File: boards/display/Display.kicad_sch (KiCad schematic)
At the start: 20 parts, among them J1 FH12-10S-0.5SH(55), J2 FH12-24S-0.5SH(55), Q1 IRLML6346

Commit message: udpate inductor
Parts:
- L1: footprint (none) -> smart_compass:L_Bourns_SRN3015BTA; Current_Rating 800mA (750mA Isat) -> 1.5A (1.0A Isat); DigiKey_PN SRN3015TA-100MCT-ND -> 118-SRN3015BTA-100MCT-ND; MPN SRN3015TA-100M -> SRN3015BTA-100M; Sourcing_Note Replaces the NR3015T100M suggested in boards/README.md, which Digi-Key now lists as Obsolete with a last-buy date of 2026-03-31. This Bourns part is the same 3.0x3.0x1.5mm shielded drum-core outline, so it should drop into the existing L_Taiyo-Yuden_NR-30xx land - verify pad geometry against the Bourns drawing before layout. -> Replaces the NR3015T100M suggested in boards/README.md, which Digi-Key lists as Obsolete with a last-buy date of 2026-03-31. The SRN3015TA considered first is marked by Bourns as not recommended for new designs, so this is the current SRN3015BTA series instead - same 3.0x3.0x1.5mm semi-shielded outline, same price, and better rated at 1.5A Irms / 1.0A Isat against 800mA / 750mA. Footprint is the Bourns recommended land from the SRN3015BTA datasheet: 3.5x3.5mm overall, 1.3mm wide pads on a 0.9mm gap, drawn as smart_compass:L_Bourns_SRN3015BTA. Note this land is larger than the 3.2x3.2mm the TA series wants and than the L_Taiyo-Yuden_NR-30xx land, so allow 3.5mm square of clear copper.
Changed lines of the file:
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@@
 			)
 		)
-		(property "Footprint" ""
+		(property "Footprint" "smart_compass:L_Bourns_SRN3015BTA"
 			(at 128.27 77.47 0)
 			(hide yes)
@@
 			)
 		)
-		(property "Datasheet" ""
+		(property "Datasheet" "https://www.bourns.com/docs/Product-Datasheets/SRN3015BTA.pdf"
 			(at 128.27 77.47 0)
 			(hide yes)
@@
 			)
 		)
-		(property "Description" "Inductor with Inductance 10uH Tol.+/-20% Package 0603 (1608)"
+		(property "Description" "10uH +/-20% semi-shielded drum-core power inductor, 1.5A Irms, 1.0A Isat, 264mOhm max, 3.0x3.0x1.5mm"
 			(at 128.27 77.47 0)
 			(hide yes)
@@
 			)
 		)
-		(property "MPN" "SRN3015TA-100M"
+		(property "MPN" "SRN3015BTA-100M"
 			(at 128.27 77.47 0)
 			(hide yes)
@@
 			)
 		)
-		(property "DigiKey_PN" "SRN3015TA-100MCT-ND"
+		(property "DigiKey_PN" "118-SRN3015BTA-100MCT-ND"
 			(at 128.27 77.47 0)
 			(hide yes)
@@
 			)
 		)
-		(property "Current_Rating" "800mA (750mA Isat)"
+		(property "Current_Rating" "1.5A (1.0A Isat)"
 			(at 128.27 77.47 0)
 			(hide yes)
@@
 			)
 		)
-		(property "Sourcing_Note" "Replaces the NR3015T100M suggested in boards/README.md, which Digi-Key now lists as Obsolete with a last-buy date of 2026-03-31. This Bourns part is the same 3.0x3.0x1.5mm shielded drum-core outline, so it should drop into the existing L_Taiyo-Yuden_NR-30xx land - verify pad geometry against the Bourns drawing before layout."
+		(property "Sourcing_Note" "Replaces the NR3015T100M suggested in boards/README.md, which Digi-Key lists as Obsolete with a last-buy date of 2026-03-31. The SRN3015TA considered first is marked by Bourns as not recommended for new designs, so this is the current SRN3015BTA series instead - same 3.0x3.0x1.5mm semi-shielded outline, same price, and better rated at 1.5A Irms / 1.0A Isat against 800mA / 750mA. Footprint is the Bourns recommended land from the SRN3015BTA datasheet: 3.5x3.5mm overall, 1.3mm wide pads on a 0.9mm gap, drawn as smart_compass:L_Bourns_SRN3015BTA. Note this land is larger than the 3.2x3.2mm the TA series wants and than the L_Taiyo-Yuden_NR-30xx land, so allow 3.5mm square of clear copper."
 			(at 128.27 77.47 0)
 			(hide yes)

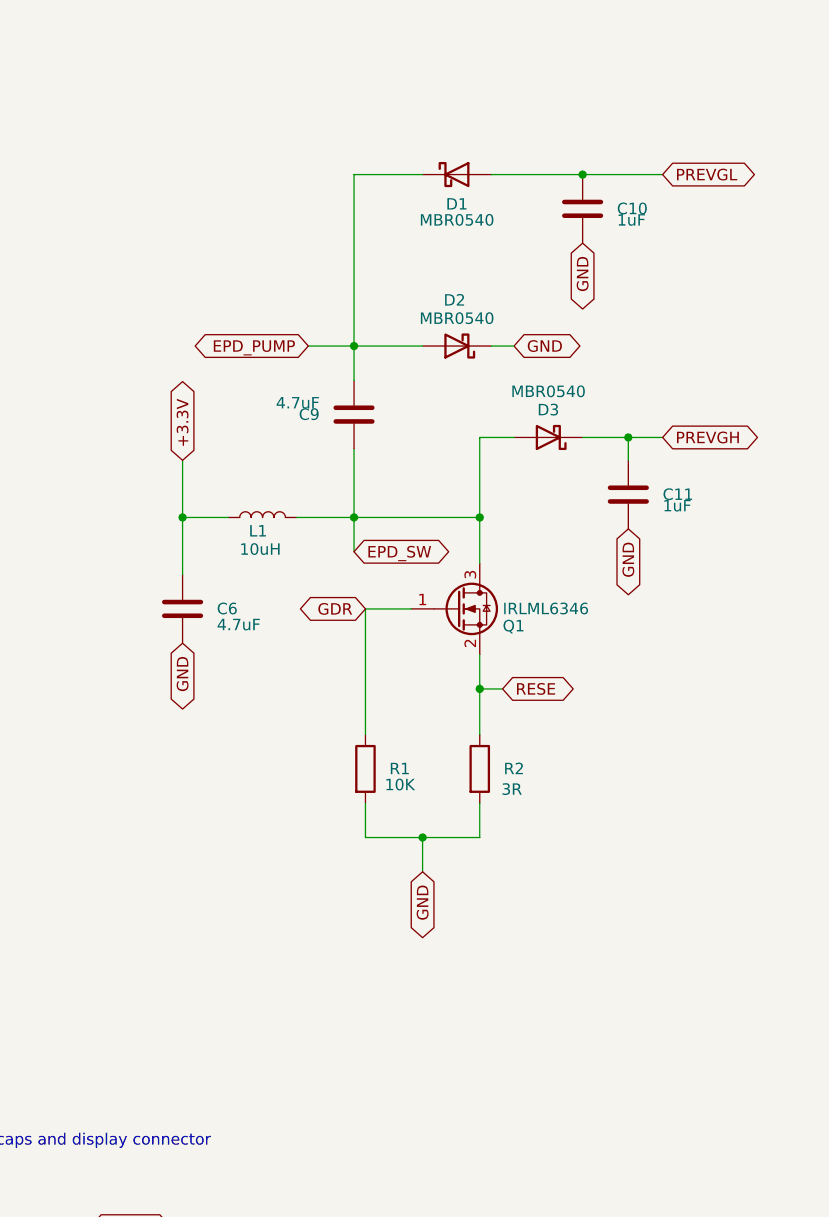
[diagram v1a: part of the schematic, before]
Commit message: grab a bunch of datasheets. Fix some models, fix some footprints, replace an unsuited capacitor
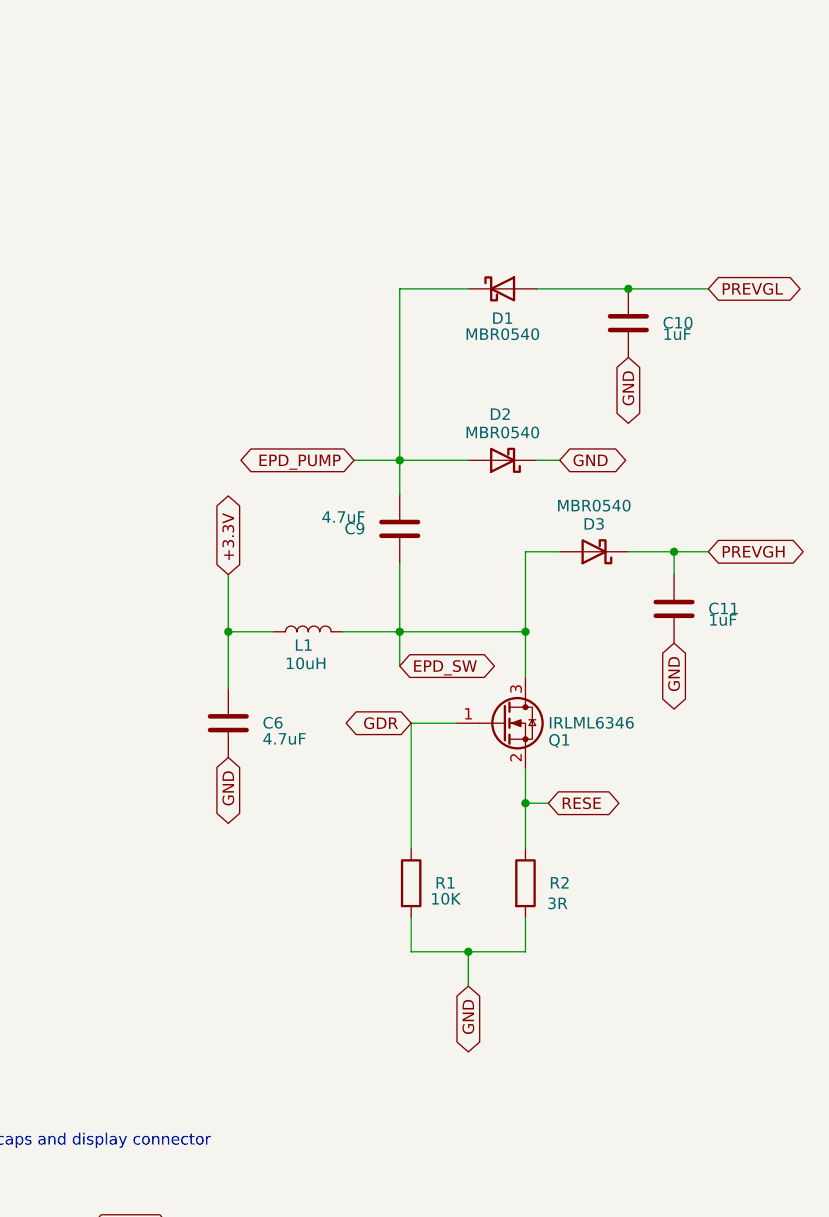
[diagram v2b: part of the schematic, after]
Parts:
- C6: footprint Capacitor_SMD:C_0402_1005Metric -> Capacitor_SMD:C_1206_3216Metric; Dielectric X5R -> X7R; DigiKey_PN 1276-1482-1-ND -> 1276-3179-1-ND; MPN CL05A475MP5NRNC -> CL31B475KBHNFNE; Sourcing_Note (none) -> Input capacitor on the +3.3V rail feeding the boost inducto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; Tolerance (none) -> 10%; Voltage 10V -> 50V
- C9: footprint Capacitor_SMD:C_0402_1005Metric -> Capacitor_SMD:C_1206_3216Metric; Dielectric X5R -> X7R; DigiKey_PN 1276-1482-1-ND -> 1276-3179-1-ND; MPN CL05A475MP5NRNC -> CL31B475KBHNFNE; Sourcing_Note (none) -> Flying capacitor in the panel's charge pump, coupling the b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; Tolerance (none) -> 10%; Voltage 10V -> 50V
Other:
- moved on the sheet: C10, C11, C6, C9, D1, D2, D3, L1, Q1, R1, R2

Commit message: replace symbols for a schottky diode and a mosfet
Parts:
- removed D1, D2, D3: MBR0540, Diode_SMD:D_SOD-123, symbol Diode:MBR0530
- removed Q1: IRLML6346, Package_TO_SOT_SMD:SOT-23, symbol Transistor_FET:Q_NMOS_GSD
- added D1, D2, D3: MBR0540, Diode_SMD:D_SOD-123, symbol smart_compass:MBR0540
- added Q1: IRLML6346, Package_TO_SOT_SMD:SOT-23, symbol smart_compass:IRLML6346
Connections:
- net EPD_PUMP: now also D1.1 (K), D2.2 (A)
- net EPD_SW: now also D3.2 (A), Q1.3 (D)
- net GDR: now also Q1.1 (G)
- net GND: now also D2.1 (K)
- net PREVGH: now also D3.1 (K)
- net PREVGL: now also D1.2 (A)
- net RESE: now also Q1.2 (S)

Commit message: replace capacitor that's in danger of being a bottleneck
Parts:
- C2: DigiKey_PN 1276-6456-1-ND -> 445-6970-1-ND; MPN CL21A106KPFNNNG -> CGA4J3X5R1A106K125AB; Manufacturer Samsung Electro-Mechanics -> TDK; PRICE (none) -> 0.24
